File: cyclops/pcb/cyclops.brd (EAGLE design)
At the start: 124.5 x 79.9 mm, 182 parts, among them Q4 IRF510, U1 MCP4921, U11 THS4281, U12 MAX4564, U13 ZXTD, U14 ZXTD, U15 OPA1664, U2 LT1931, U3 LT1764A, U31 TPS62153, U4 BD00IA5WEFJ-E2, U5 TPS72325, U6 LT1711, U7 TLV3701, U8 ADR03, U9 LT1880

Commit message: More routing. Very near completion.
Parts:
- removed C40: 10uF, jonnew:1206
- moved R23 48.7 mm to (52.8, 40.5)
- moved R25 45.8 mm to (49.1, 40.5), turned to 0 degrees
- moved Q2 45.6 mm to (49.0, 44.6)
- moved C26 28.7 mm to (62.2, 63.5), turned to 0 degrees
- moved -5V 28.3 mm to (44.5, 40.3)
- moved REF5V0 24.0 mm to (63.5, 60.7)
- moved R35 21.9 mm to (34.8, 11.6), turned to 90 degrees
- moved R52 9.37 mm to (77.0, 51.9), turned to 180 degrees
- moved L2 9.33 mm to (32.9, 49.7)
- moved REF2V5 7.11 mm to (51.2, 64.3)
- moved R5 5.16 mm to (73.4, 51.9)
- moved C20 4.58 mm to (57.9, 45.2)
- moved C21 4.58 mm to (52.1, 45.2)
- moved R18 4.58 mm to (58.7, 40.5)
- moved R19 4.58 mm to (55.8, 39.4)
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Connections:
- net N$50 renamed ~LED_ACTIVE
- removed net N$48: D6.A
- removed net N$53: D5.C
- net +13.3V: no longer C40.1
- net +6V: now also D5.C
- net GND: now also D6.A; no longer C40.2
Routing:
- net +13.3V: track 27.1 -> 170.6 mm, vias 206 -> 205
- net LED_ACTIVE: track 5.23 -> 77.4 mm, vias 2 -> 4
- net VAUX: track 23.2 -> 74.7 mm
- net N$47: track 9.84 -> 61.3 mm, vias 0 -> 2
- net VI: track 16.3 -> 67.2 mm
- net REF5.0: track 23.5 -> 71.2 mm, vias 1 -> 2
- net VREF: track 17.9 -> 61.3 mm
- net VI_INTERNAL: track 2.16 -> 44.6 mm, vias 0 -> 2
- net N$37: track 27.3 -> 58.2 mm
- net VAUX_OUT: track 17.2 -> 46.7 mm, vias 2 -> 4
- net REF2.5: track 17.1 -> 41.9 mm, vias 1 -> 2
- net OVER_CURR: track 0.00 -> 16.8 mm, vias 0 -> 2
- net -5V: track 0.00 -> 9.85 mm
- net OVER_CURR_PRE: track 44.7 -> 36.6 mm
- net N$11: track 0.00 -> 7.76 mm
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
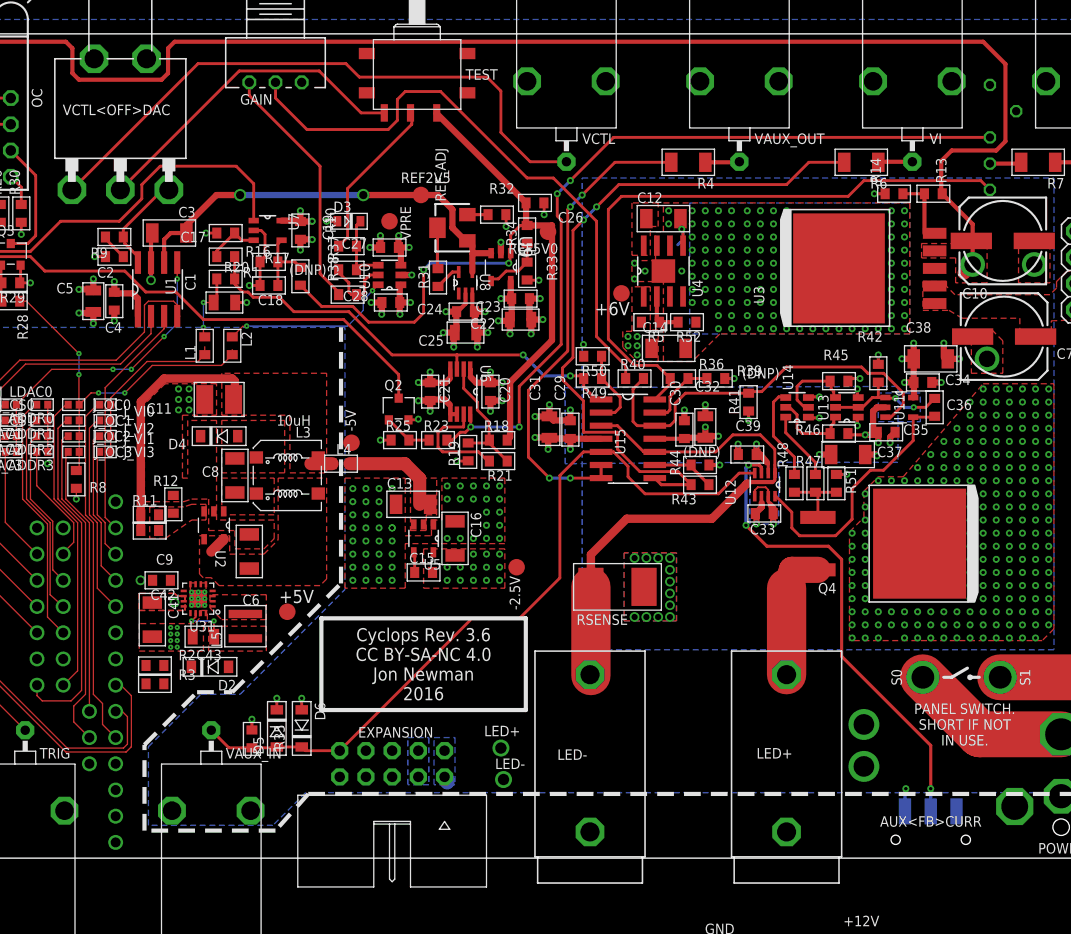
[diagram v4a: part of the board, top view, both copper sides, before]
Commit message: More routing. Need to do ERC/DRC at this point.
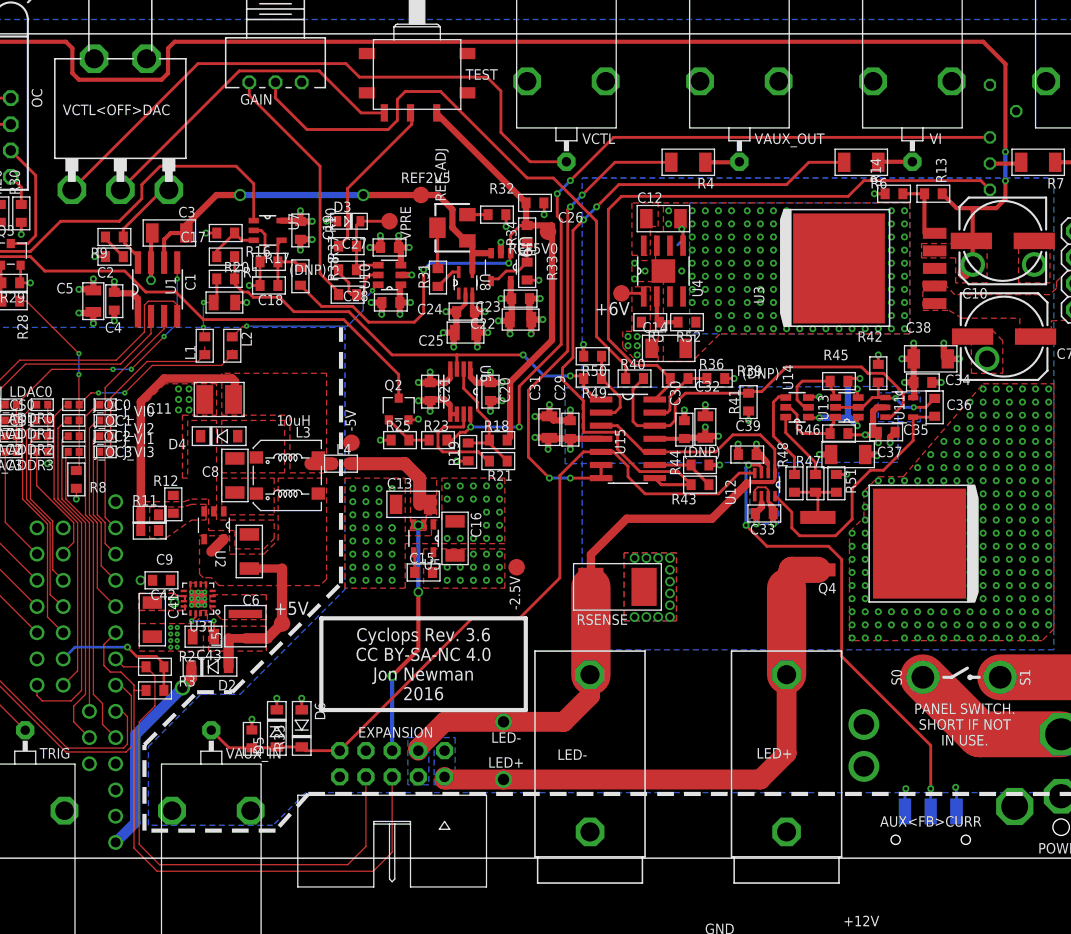
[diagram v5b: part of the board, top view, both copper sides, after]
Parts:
- moved +5V 1.25 mm to (37.7, 22.7)
- moved R3 0.63 mm to (25.4, 16.3)
- moved R2 0.13 mm to (25.4, 18.5)
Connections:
- net +13.3V: no longer EXPANSION.7
- net +6V: now also EXPANSION.7
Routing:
- net SDA: track 0.00 -> 58.3 mm
- net SCL: track 0.00 -> 51.7 mm
- net LED+: track 13.4 -> 55.4 mm
- net -5V: track 9.85 -> 32.7 mm, vias 0 -> 3
- net LED-: track 55.2 -> 76.2 mm
- net TEENSY_VIN: track 0.00 -> 20.1 mm, vias 0 -> 1
- net +5V: track 6.31 -> 23.4 mm
- net +3V3: track 0.00 -> 13.5 mm, vias 0 -> 1
- net +13.3V: track 170.6 -> 178.0 mm, vias 205 -> 207
- net GND: track 97.1 -> 100.7 mm, vias 258 -> 259
- net VCTL: track 7.14 -> 9.96 mm
- net +6V: track 54.6 -> 56.9 mm

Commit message: Started ERC/DRC process.
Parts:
- added +13.3V, GND: RCU-0C, jonnew:RC0603
- +5V, +6V, -2.5V, -5V, REF2V5, REF5V0: value TPTP16R -> RCU-0C; device cyclops:TP16R -> jonnew:RC0603
- IND, OC: value (none) -> 569-0112-200
- Q1, Q2, Q3: value (none) -> SSM3K324
- U10: value (none) -> ADG1201
- moved -5V 3.45 mm to (47.2, 38.2), turned to 90 degrees
- moved REF5V0 0.39 mm to (63.9, 60.7), turned to 180 degrees
- moved -2.5V 0.13 mm to (60.3, 28.2), turned to 180 degrees
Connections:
- removed net AGND: UC.AGND
- removed net AREF: UC.AREF
- net +13.3V: now also +13.3V.1
- net +5V: now also +5V.1; no longer +5V.TP
- net +6V: now also +6V.1; no longer +6V.TP
- net -2.5V: now also -2.5V.1; no longer -2.5V.TP
- net -5V: now also -5V.1; no longer -5V.TP
- net GND: now also GND.1, UC.AGND
- net REF2.5: now also REF2V5.1; no longer REF2V5.TP
- net REF5.0: now also REF5V0.1; no longer REF5V0.TP
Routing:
- net SCL: track 51.7 -> 64.6 mm, vias 0 -> 3
- net SDA: track 58.3 -> 64.5 mm, vias 0 -> 1
- net +13.3V: track 178.0 -> 173.8 mm, vias 207 -> 208
- net LED-: track 76.2 -> 79.5 mm
- net LED+: track 55.4 -> 57.4 mm
- net -2.5V: track 31.8 -> 33.3 mm
- net GND: track 100.7 -> 102.2 mm
- removed copper zone on layer 16, net LED+
- removed copper zone on layer 16, net LED-
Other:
- board text added: "+13.3V"
- board text added: "TEST/SOLDER POINT SINKSCREEN GO ON TOP AND BOTTOM!"
